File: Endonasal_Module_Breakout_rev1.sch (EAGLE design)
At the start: 43 parts, among them M0_LIMIT_XOR XOR-SOT353, M3_LIMIT_XOR XOR-SOT353

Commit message: All traces routed
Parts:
- removed M0_LEDG, M1_LEDG, M2_LEDG, M3_LEDG, M4_LEDG, M5_LEDG: (no value), Cannula_1_0:LED-0805
- removed R2, R3, R4, R5, R6: 220, Cannula_1_0:RESISTOR-0603
- added POWER_LEDG: (no value), Cannula_1_0:LED-0805
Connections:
- removed net N$1: M5_LEDG.A, R6.1
- removed net N$2: M4_LEDG.A, R5.1
- removed net N$3: M3_LEDG.A, R4.1
- removed net N$4: M2_LEDG.A, R3.1
- removed net N$5: M1_LEDG.A, R2.1
- net GND: now also POWER_LEDG.C; no longer M0_LEDG.C, M1_LEDG.C, M2_LEDG.C, M3_LEDG.C, M4_LEDG.C, M5_LEDG.C
- net M0_VHALL: now also R1.2
- net M2_VHALL: no longer R1.2, R2.2, R3.2
- net M3_VHALL: no longer R4.2
- net M4_VHALL: no longer R5.2
- net M5_HALL1: now also R19B.1; no longer R19A.1
- net M5_HALL2: now also R19A.1; no longer R19B.1
- net M5_VHALL: no longer R6.2
- net N$6: now also POWER_LEDG.A; no longer M0_LEDG.A
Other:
- note added: "LED on when ESCON amp is powered"
- note removed: "LEDs on when ESCON amps are powered"
- moved on the sheet: C1, C2, C3, C4, C5, C6, C7, C8, C9, LIMIT, M0_LIMIT_XOR_GATE, M0_LIMIT_XOR_PWR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

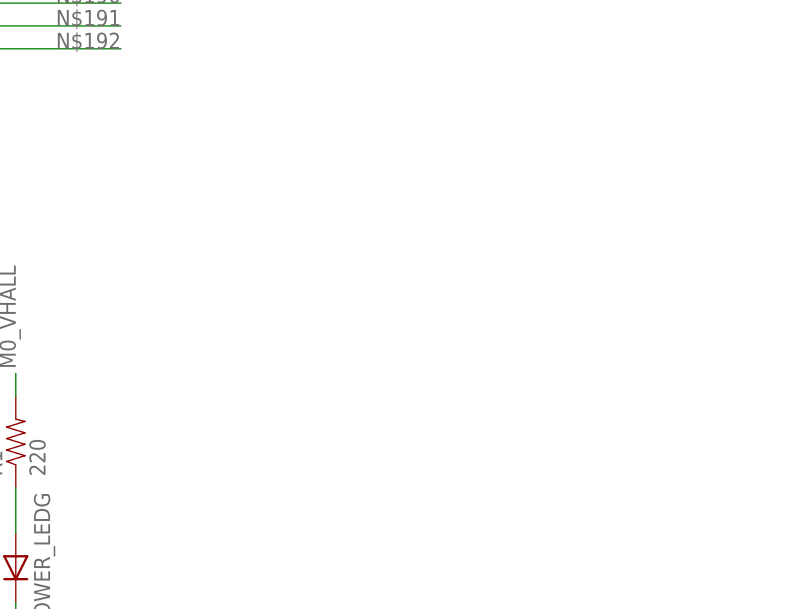
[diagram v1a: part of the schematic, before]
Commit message: Increased connector spacing
Increased spacing between connectors to be at least 5mm
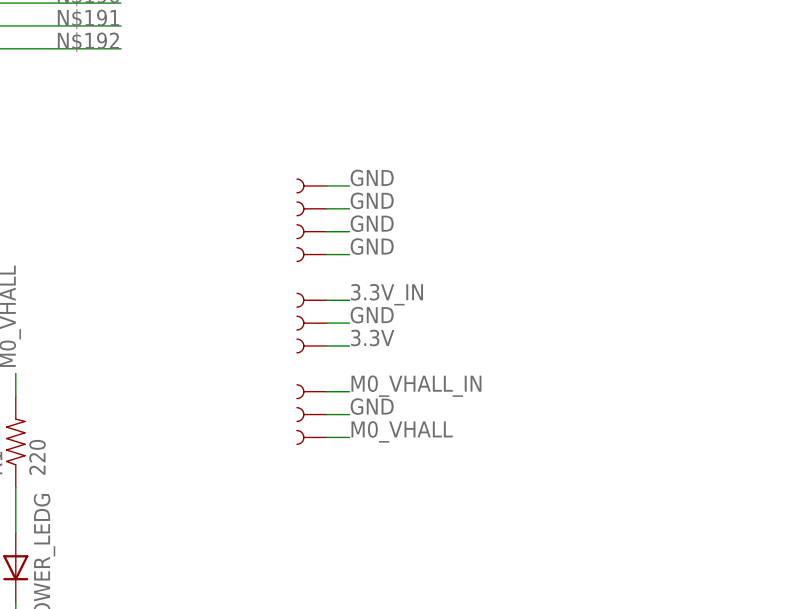
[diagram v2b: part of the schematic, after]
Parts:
- added 3.3V, 3.3V_IN, 3.3V_IN_GND, M0_VHALL, M0_VHALL_GND, M0_VHALL_IN: TEST-POINT_5021, Cannula_1_0:TEST-POINT_5021
- added TP1, TP2, TP3, TP4: TEST-POINT3X5, Cannula_1_0:TEST-POINT3X5
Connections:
- net 3.3V: now also 3.3V.1
- net 3.3V_IN: now also 3.3V_IN.1
- net GND: now also 3.3V_IN_GND.1, M0_VHALL_GND.1, TP1.1, TP2.1, TP3.1, TP4.1
- net M0_VHALL: now also M0_VHALL.1
- net M0_VHALL_IN: now also M0_VHALL_IN.1
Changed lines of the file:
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@@
 <part name="R18" library="SparkFun-Passives" deviceset="RESISTOR-ARRAY" device="0603-ARV"/>
 <part name="R19" library="SparkFun-Passives" deviceset="RESISTOR-ARRAY" device="0603-ARV"/>
+<part name="TP1" library="Cannula_1_0" deviceset="TEST-POINT" device="3X5"/>
+<part name="TP2" library="Cannula_1_0" deviceset="TEST-POINT" device="3X5"/>
+<part name="TP3" library="Cannula_1_0" deviceset="TEST-POINT" device="3X5"/>
+<part name="TP4" library="Cannula_1_0" deviceset="TEST-POINT" device="3X5"/>
+<part name="3.3V_IN" library="Cannula_1_0" deviceset="TEST-POINT" device="_5021"/>
+<part name="3.3V_IN_GND" library="Cannula_1_0" deviceset="TEST-POINT" device="_5021"/>
+<part name="3.3V" library="Cannula_1_0" deviceset="TEST-POINT" device="_5021"/>
+<part name="M0_VHALL_IN" library="Cannula_1_0" deviceset="TEST-POINT" device="_5021"/>
+<part name="M0_VHALL" library="Cannula_1_0" deviceset="TEST-POINT" device="_5021"/>
+<part name="M0_VHALL_GND" library="Cannula_1_0" deviceset="TEST-POINT" device="_5021"/>
 </parts>
 <sheets>
@@
 <instance part="R19" gate="C" x="55.88" y="-50.8"/>
 <instance part="R19" gate="D" x="111.76" y="81.28" rot="R90"/>
+<instance part="TP1" gate="G$1" x="30.48" y="-109.22" smashed="yes" rot="R180"/>
+<instance part="TP2" gate="G$1" x="30.48" y="-111.76" smashed="yes" rot="R180"/>
+<instance part="TP3" gate="G$1" x="30.48" y="-114.3" smashed="yes" rot="R180"/>
+<instance part="TP4" gate="G$1" x="30.48" y="-116.84" smashed="yes" rot="R180"/>
+<instance part="3.3V_IN" gate="G$1" x="30.48" y="-121.92" smashed="yes" rot="R180"/>
+<instance part="3.3V_IN_GND" gate="G$1" x="30.48" y="-124.46" smashed="yes" rot="R180"/>
+<instance part="3.3V" gate="G$1" x="30.48" y="-127" smashed="yes" rot="R180"/>
+<instance part="M0_VHALL_IN" gate="G$1" x="30.48" y="-132.08" smashed="yes" rot="R180"/>
+<instance part="M0_VHALL" gate="G$1" x="30.48" y="-137.16" smashed="yes" rot="R180"/>
+<instance part="M0_VHALL_GND" gate="G$1" x="30.48" y="-134.62" smashed="yes" rot="R180"/>
 </instances>
 <busses>
@@
 <wire x1="-27.94" y1="-154.94" x2="-27.94" y2="-157.48" width="0.1524" layer="91"/>
 </segment>
+<segment>
+<pinref part="TP1" gate="G$1" pin="1"/>
+<wire x1="30.48" y1="-109.22" x2="33.02" y2="-109.22" width="0.1524" layer="91"/>
+<label x="33.02" y="-109.22" size="1.778" layer="95"/>
+</segment>
+<segment>
+<pinref part="TP2" gate="G$1" pin="1"/>
+<wire x1="30.48" y1="-111.76" x2="33.02" y2="-111.76" width="0.1524" layer="91"/>
+<label x="33.02" y="-111.76" size="1.778" layer="95"/>
+</segment>
+<segment>
+<pinref part="TP3" gate="G$1" pin="1"/>
+<wire x1="30.48" y1="-114.3" x2="33.02" y2="-114.3" width="0.1524" layer="91"/>
+<label x="33.02" y="-114.3" size="1.778" layer="95"/>
+</segment>
+<segment>
+<pinref part="TP4" gate="G$1" pin="1"/>
+<wire x1="30.48" y1="-116.84" x2="33.02" y2="-116.84" width="0.1524" layer="91"/>
+<label x="33.02" y="-116.84" size="1.778" layer="95"/>
+</segment>
+<segment>
+<pinref part="3.3V_IN_GND" gate="G$1" pin="1"/>
+<wire x1="30.48" y1="-124.46" x2="33.02" y2="-124.46" width="0.1524" layer="91"/>
+<label x="33.02" y="-124.46" size="1.778" layer="95"/>
+</segment>
+<segment>
+<pinref part="M0_VHALL_GND" gate="G$1" pin="1"/>
+<wire x1="30.48" y1="-134.62" x2="33.02" y2="-134.62" width="0.1524" layer="91"/>
+<label x="33.02" y="-134.62" size="1.778" layer="95"/>
+</segment>
 </net>
 <net name="3.3V" class="0">
@@
 <wire x1="-25.4" y1="-144.78" x2="-27.94" y2="-144.78" width="0.1524" layer="91"/>
 <junction x="-27.94" y="-144.78"/>
+</segment>
+<segment>
+<pinref part="3.3V" gate="G$1" pin="1"/>
+<wire x1="30.48" y1="-127" x2="33.02" y2="-127" width="0.1524" layer="91"/>
+<label x="33.02" y="-127" size="1.778" layer="95"/>
 </segment>
 </net>
@@
 <label x="-4.064" y="-129.54" size="1.778" layer="95" rot="R90"/>
 </segment>
+<segment>
+<pinref part="M0_VHALL" gate="G$1" pin="1"/>
+<wire x1="30.48" y1="-137.16" x2="33.02" y2="-137.16" width="0.1524" layer="91"/>
+<label x="33.02" y="-137.16" size="1.778" layer="95"/>
+</segment>
 </net>
 <net name="M0_ENC_A" class="0">
@@
 <label x="-132.08" y="-131.826" size="1.778" layer="95" rot="R90"/>
 </segment>
+<segment>
+<pinref part="M0_VHALL_IN" gate="G$1" pin="1"/>
+<wire x1="30.48" y1="-132.08" x2="33.02" y2="-132.08" width="0.1524" layer="91"/>
+<label x="33.02" y="-132.08" size="1.778" layer="95"/>
+</segment>
 </net>
 <net name="M1_VHALL_IN" class="0">
@@
 <label x="-27.94" y="-129.286" size="1.778" layer="95" rot="R90"/>
 </segment>
-</net>
+<segment>
+<pinref part="3.3V_IN" gate="G$1" pin="1"/>
+<wire x1="30.48" y1="-121.92" x2="33.02" y2="-121.92" width="0.1524" layer="91"/>
+<label x="33.02" y="-121.92" size="1.778" layer="95"/>
+</segment>
+</net>

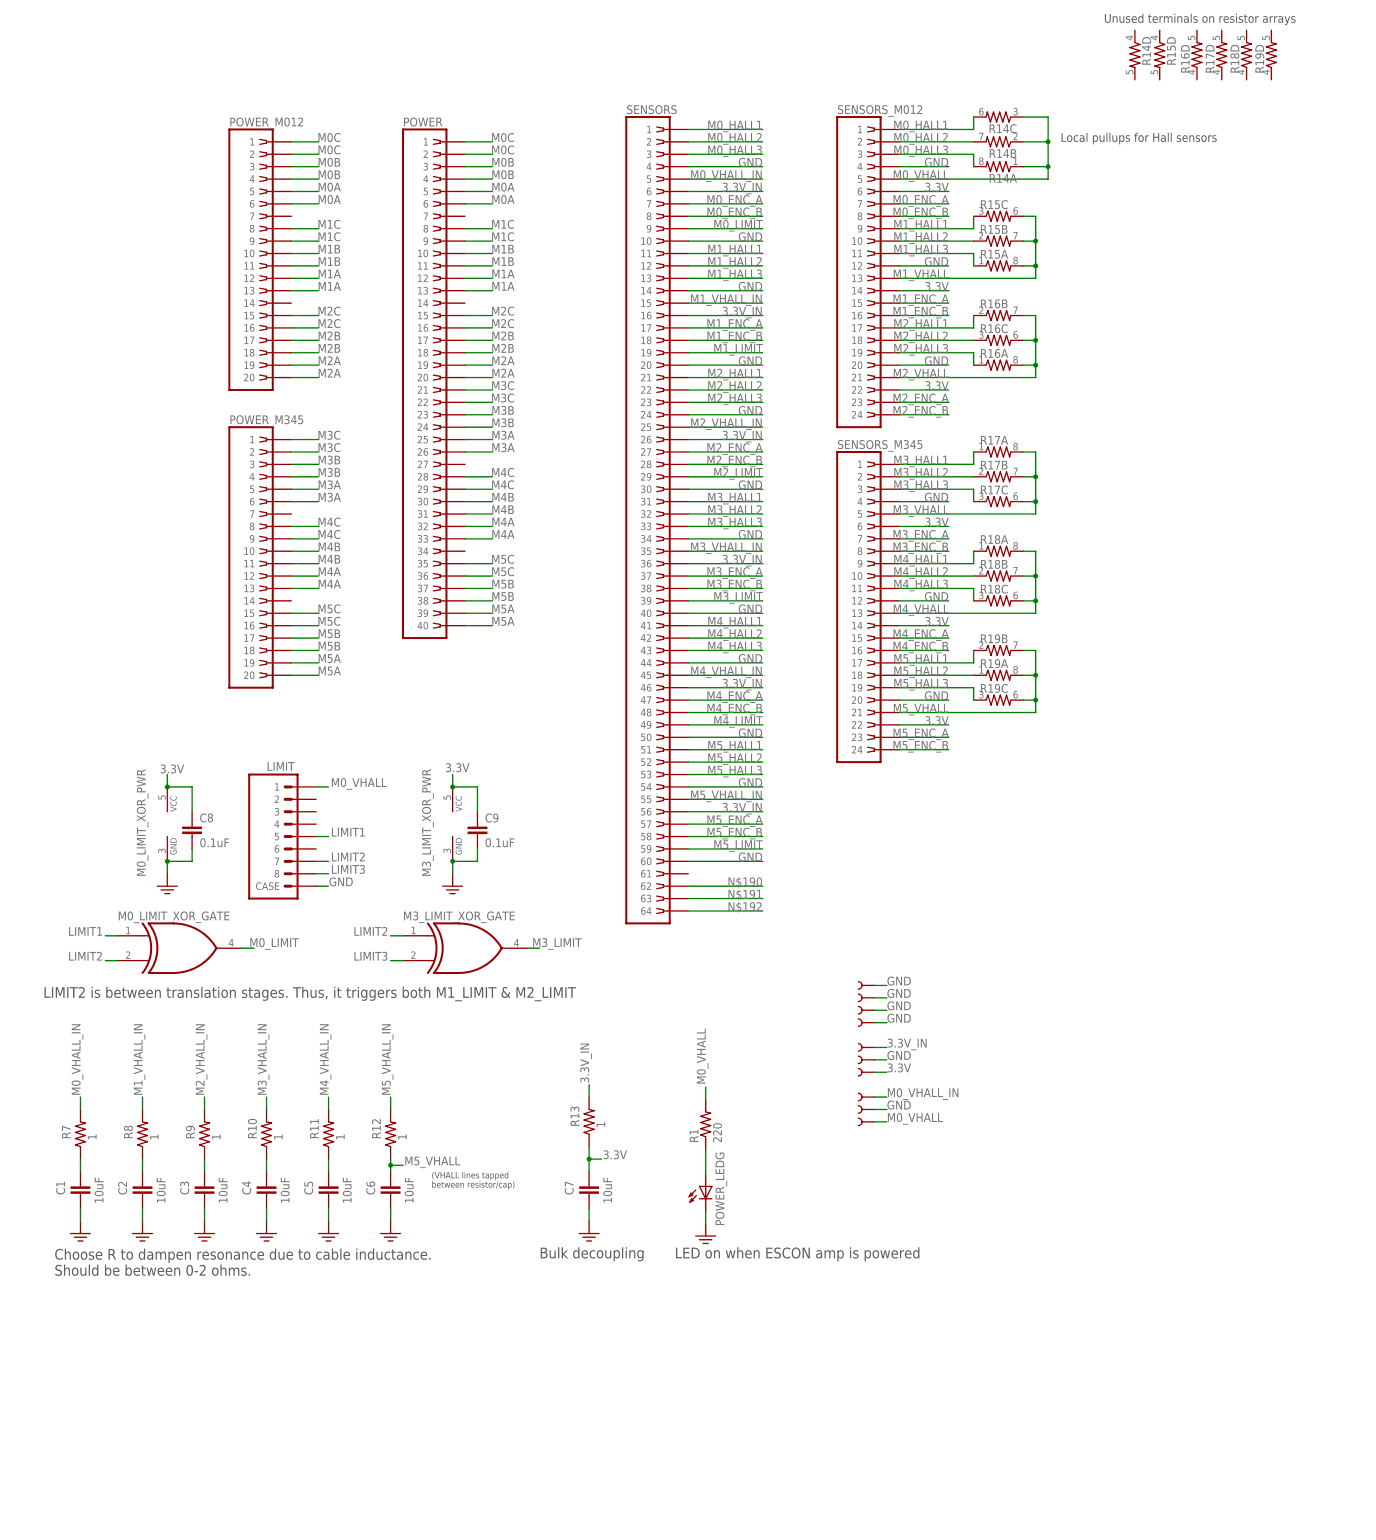
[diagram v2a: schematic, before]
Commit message: Silkscreen
Set font sizes for passives
Renumbered components
Created net classes for POWER and MOTOR
Ran DRC and ERC
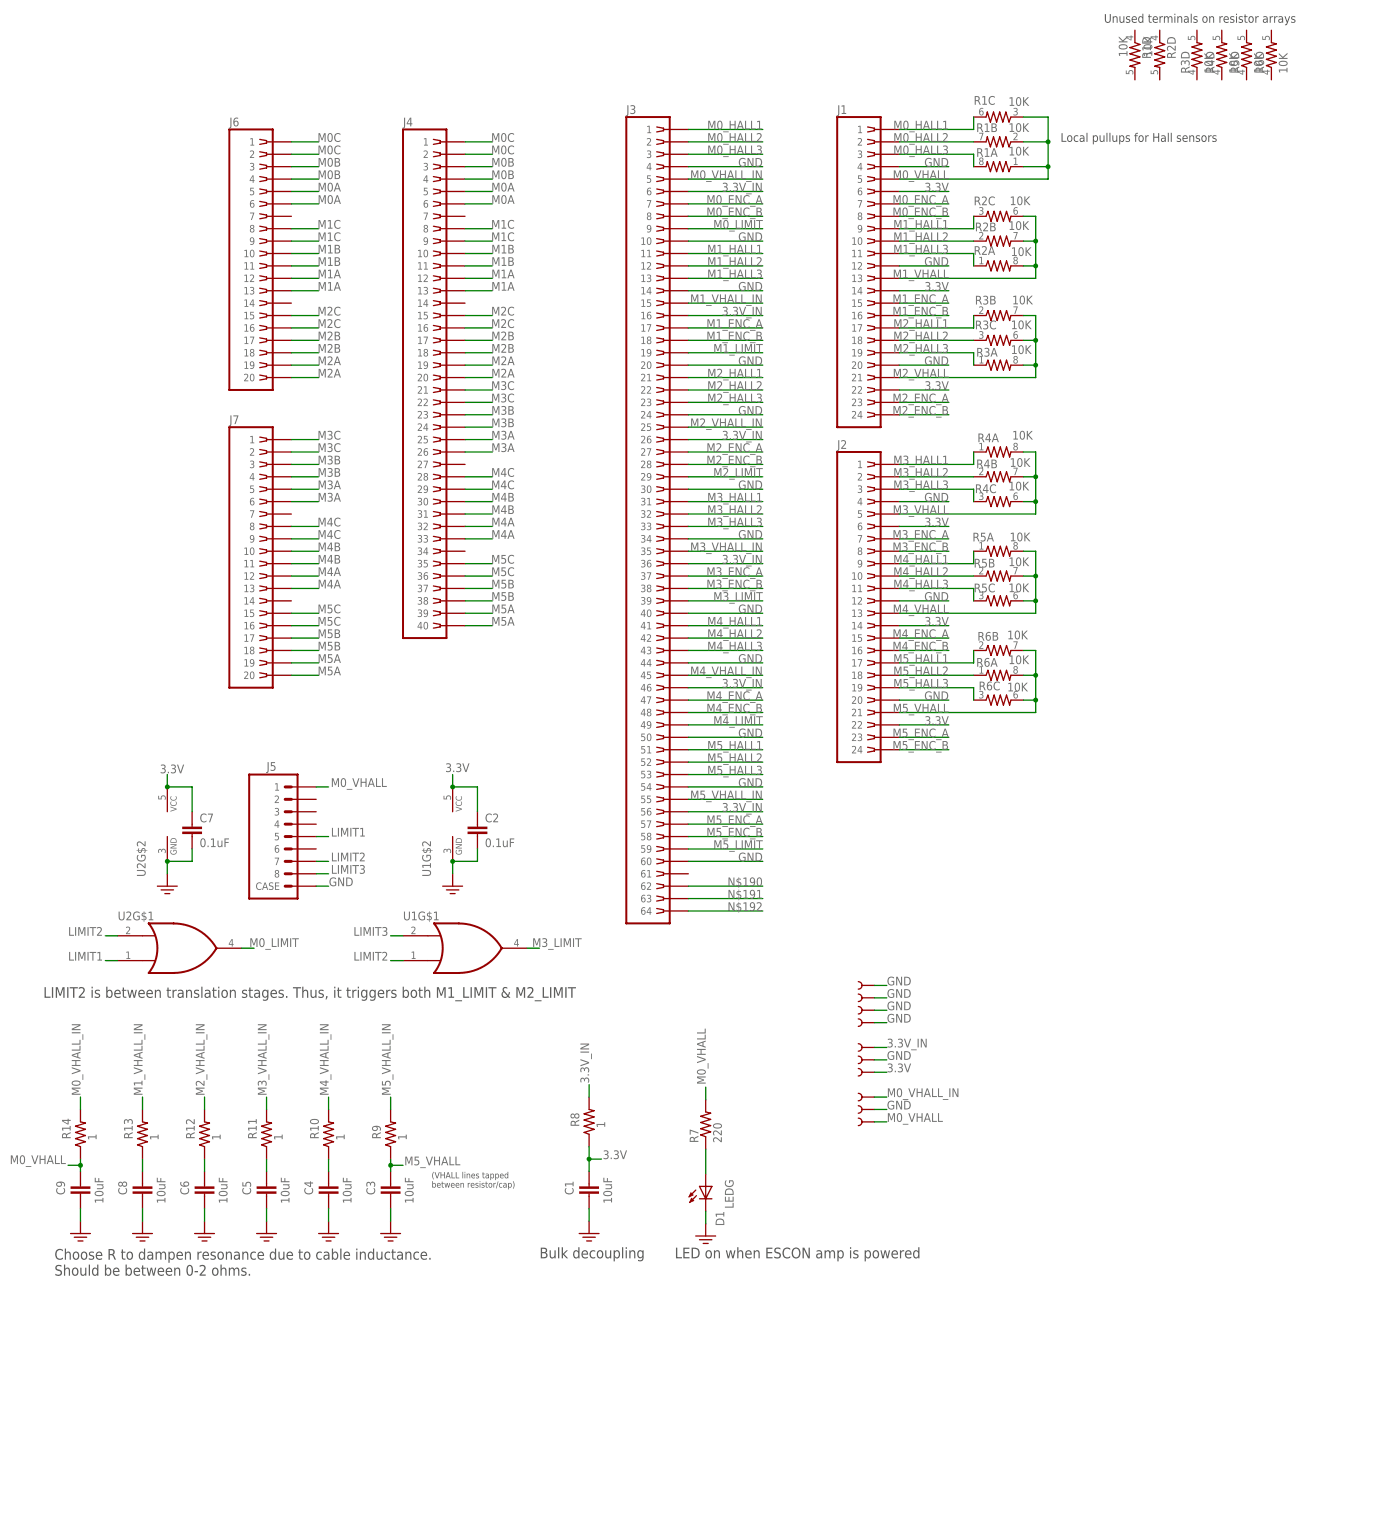
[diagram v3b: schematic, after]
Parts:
- removed 3.3V, M0_VHALL, M0_VHALL_GND, M0_VHALL_IN: TEST-POINT_5021, Cannula_1_0:TEST-POINT_5021
- removed M0_LIMIT_XOR, M3_LIMIT_XOR: XOR-SOT353, Cannula_1_0:XOR-SOT353
- added TP10, TP7, TP8, TP9: TEST-POINT3X5, Cannula_1_0:TEST-POINT3X5
- added U1: OR_M3, Cannula_1_0:OR
- added U2: OR_M0, Cannula_1_0:OR
- C2, C7: value 10uF -> 0.1uF; device Cannula_1_0:CAP0805 -> SparkFun-Capacitors:CAP0603-CAP
- C8, C9: value 0.1uF -> 10uF; device SparkFun-Capacitors:CAP0603-CAP -> Cannula_1_0:CAP0805
- D1: value (none) -> LEDG
- R1: value 220 -> 10K; device Cannula_1_0:RESISTOR-0603 -> SparkFun-Passives:RESISTOR-ARRAY0603-ARV
- R14: value (none) -> 1; device SparkFun-Passives:RESISTOR-ARRAY0603-ARV -> Cannula_1_0:RESISTOR-0603
- R2, R3, R4, R5, R6: value (none) -> 10K
- R7: value 1 -> 220
- TP1, TP2, TP3, TP4: value TEST-POINT3X5 -> TEST-POINT_5021; device Cannula_1_0:TEST-POINT3X5 -> Cannula_1_0:TEST-POINT_5021
- renumbered 3.3V_IN to TP6, 3.3V_IN_GND to TP5, LIMIT to J5, POWER to J4, POWER_LEDG to D1, POWER_M012 to J6, POWER_M345 to J7, R15 to R2, R16 to R3, R17 to R4, R18 to R5, R19 to R6, SENSORS to J3, SENSORS_M012 to J1, SENSORS_M345 to J2
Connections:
- net 3.3V: now also C1.1, C2.1, R8.1, TP4.1, U1G$2.VCC, U2G$2.VCC; no longer 3.3V.1, C8.1, C9.1, M0_LIMIT_XOR_PWR.VCC, M3_LIMIT_XOR_PWR.VCC, R13.1
- net 3.3V_IN: now also R8.2; no longer R13.2
- net GND: now also TP10.1, TP7.1, TP8.1, TP9.1, U1G$2.GND, U2G$2.GND; no longer M0_LIMIT_XOR_PWR.GND, M0_VHALL_GND.1, M3_LIMIT_XOR_PWR.GND, TP1.1, TP3.1, TP4.1
- net LIMIT1: now also U2G$1.B; no longer M0_LIMIT_XOR_GATE.A
- net LIMIT2: now also U1G$1.B, U2G$1.A; no longer M0_LIMIT_XOR_GATE.B, M3_LIMIT_XOR_GATE.A
- net LIMIT3: now also U1G$1.A; no longer M3_LIMIT_XOR_GATE.B
- net M0_HALL1: now also R1C.2; no longer R14C.2
- net M0_HALL2: now also R1B.2; no longer R14B.2
- net M0_HALL3: now also R1A.2; no longer R14A.2
- net M0_LIMIT: now also U2G$1.Y; no longer M0_LIMIT_XOR_GATE.Y
- net M0_VHALL: now also C9.1, R14.1, R1A.1, R1B.1, R1C.1, R7.2, TP1.1; no longer C1.1, M0_VHALL.1, R1.2, R14A.1, R14B.1, R14C.1, R7.1
- net M0_VHALL_IN: now also R14.2, TP3.1; no longer M0_VHALL_IN.1, R7.2
- net M1_VHALL: now also C8.1, R13.1; no longer C2.1, R8.1
- net M1_VHALL_IN: now also R13.2; no longer R8.2
- net M2_VHALL: now also C6.1, R12.1; no longer C3.1, R9.1
- net M2_VHALL_IN: now also R12.2; no longer R9.2
- net M3_LIMIT: now also U1G$1.Y; no longer M3_LIMIT_XOR_GATE.Y
- net M3_VHALL: now also C5.1, R11.1; no longer C4.1, R10.1
- net M3_VHALL_IN: now also R11.2; no longer R10.2
- net M4_VHALL: now also C4.1, R10.1; no longer C5.1, R11.1
- net M4_VHALL_IN: now also R10.2; no longer R11.2
- net M5_VHALL: now also C3.1, R9.1; no longer C6.1, R12.1
- net M5_VHALL_IN: now also R9.2; no longer R12.2
- net N$6: now also R7.1; no longer R1.1
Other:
- moved on the sheet: C1, C2, C3, C4, C5, C6, C7, C8, C9, R10, R11, R12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
